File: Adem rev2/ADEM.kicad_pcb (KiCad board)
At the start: 2 copper layers, 29 parts, among them P1 CONN_buzz, P2 CONN_01X03, P3 CONN_01X04, Q1 NPN, U3 ESP8266_THING, U4 MPU6050, U5 NVSRAM, U6 BMP180, U7 HTU21D

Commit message: added adem logo's
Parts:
- added G***: LOGO, Adem_Kicad_logos:adem_logo, F.Cu at (152.0, 138.0)
- added G***: LOGO, Adem_Kicad_logos:adem_logo-txt_17_B_silk, F.Cu at (177.0, 138.8)
- moved C2 2.22 mm to (147.3, 116.3)
- moved Q1 0.36 mm to (203.1, 142.6)
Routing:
- net GND: track 93.2 -> 60.2 mm
- net (no net): track 50.0 -> 64.0 mm
- net VCC: track 75.2 -> 70.6 mm
- added copper zone on F.Cu, net GND
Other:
- board outline added: 69 x 49 mm
- board text added: "github.com/timelab/ADEM-hardware github.com/timelab/ADEM www.ik-adem.be"

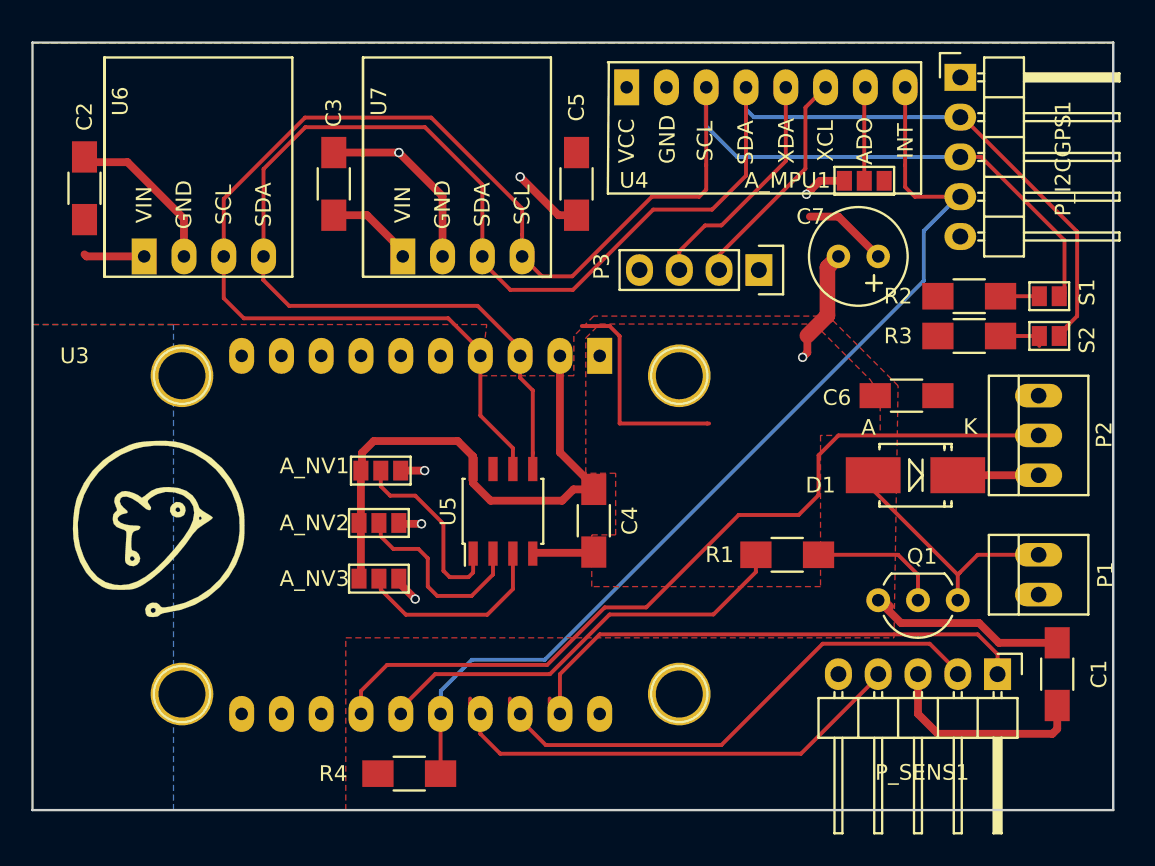
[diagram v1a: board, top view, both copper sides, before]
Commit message: added mounting hole and fixed footprint error
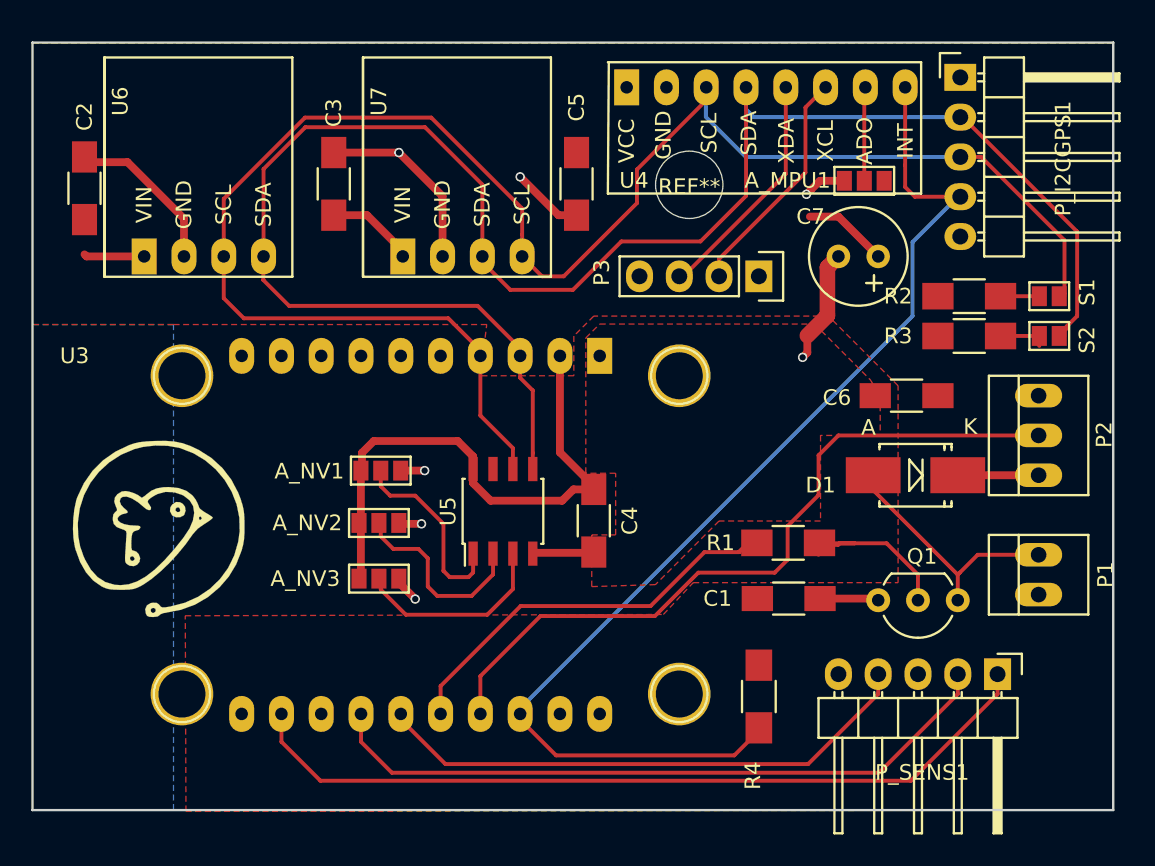
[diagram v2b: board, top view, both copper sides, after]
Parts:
- added REF**: MountingHole_4.3mm_M4, Mounting_Holes:MountingHole_4.3mm_M4, F.Cu at (185.9, 116.1)
- moved R4 22.9 mm to (190.4, 148.7), turned to 270 degrees
- moved C1 17.8 mm to (192.3, 142.5), turned to 0 degrees
- moved R1 0.76 mm to (192.2, 138.9)
- moved P3 0.40 mm to (190.4, 121.9)
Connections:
- U3 pad 11: GND -> Net-(U3-Pad11)
- U3 pad 12: Net-(U3-Pad12) -> A_SENSOR
- U3 pad 14: NEO_PXL -> P10_SENS
- U3 pad 15: BUZZ -> P25_SENS
- U3 pad 16: INT -> BUZZ
- U3 pad 17: P25_SENS -> NEO_PXL
- U3 pad 18: P10_SENS -> INT
- U3 pad 19: A_SENSOR -> Net-(U3-Pad19)
- U3 pad 20: Net-(U3-Pad20) -> GND
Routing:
- net A_SENSOR: track 33.7 -> 52.1 mm
- net (no net): track 64.0 -> 50.0 mm
- net VCC: track 70.6 -> 57.0 mm
- net P10_SENS: track 32.9 -> 44.2 mm
- net GND: track 60.2 -> 50.5 mm
- net INT: track 63.9 -> 72.4 mm
- net P25_SENS: track 30.1 -> 35.6 mm
- net NEO_PXL: track 53.0 -> 47.5 mm
- net Net-(Q1-Pad2): track 8.51 -> 11.4 mm
- net SCL: track 112.3 -> 109.8 mm
- net BUZZ: track 28.1 -> 26.6 mm
- net SDA: track 114.4 -> 115.2 mm
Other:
- board text added: "www.ik-adem.be github.com/timelab/ADEM github.com/timelab/ADEM-hardware"
- board text removed: "github.com/timelab/ADEM-hardware github.com/timelab/ADEM www.ik-adem.be"

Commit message: alfa prototype
updated for first pcb prototype
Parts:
- added 5V1: 5V, Connect:PINHEAD1-2, F.Cu at (208.9, 153.5)
- added D2: 1V8, Diodes_SMD:D_1206, F.Cu at (196.6, 152.8)
- added D3: 1V8, Diodes_SMD:D_1206, F.Cu at (196.6, 150.4)
- added R5: 10K, Resistors_SMD:R_1206_HandSoldering, F.Cu at (165.3, 146.9)
- added R6: 10K, Resistors_SMD:R_1206_HandSoldering, F.Cu at (165.4, 144.3)
- added VCC_SEL1: GS_VCC, Connect:GS3, B.Cu at (205.0, 150.9)
- ? (x2): renamed from G***; value LOGO -> (none)
- P_SENS1: footprint Pin_Headers:Pin_Header_Angled_1x05 -> Pin_Headers:Pin_Header_Straight_1x05_Pitch2.54mm
- S1: value GS1 -> S1
- moved ? 2.15 mm to (176.2, 140.8)
- moved Q1 1.63 mm to (203.0, 141.0)
- moved P_SENS1 1.32 mm to (205.6, 146.0)
- moved ? 1.20 mm to (150.8, 137.9)
- moved R4 0.58 mm to (190.4, 148.2)
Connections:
- P_SENS1 pad 3: VCC -> Net-(P_SENS1-Pad3)
- U3 pad 14: P10_SENS -> P10_SENS_SHFT
- U3 pad 15: P25_SENS -> P25_SENS_SHFT
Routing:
- net P25_SENS_SHFT: track 0.00 -> 37.7 mm
- net P10_SENS_SHFT: track 0.00 -> 36.0 mm
- net P10_SENS: track 44.2 -> 9.31 mm
- net P25_SENS: track 35.6 -> 4.41 mm
- net VCC: track 57.0 -> 76.5 mm
- net Net-(P_SENS1-Pad3): track 0.00 -> 7.21 mm
- net GND: track 50.5 -> 56.1 mm
- net Net-(5V1-Pad2): track 0.00 -> 5.16 mm
- net Net-(A_NV2-Pad2): track 12.5 -> 10.8 mm
- net Net-(D1-Pad2): track 15.9 -> 14.3 mm
- net Net-(Q1-Pad2): track 11.4 -> 9.81 mm
- net A_SENSOR: track 52.1 -> 53.2 mm
- net Net-(A_NV1-Pad2): track 12.4 -> 11.8 mm
- net BUZZ: track 26.6 -> 26.1 mm
